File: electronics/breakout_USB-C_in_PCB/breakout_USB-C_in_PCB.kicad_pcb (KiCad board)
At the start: 2 copper layers, 29 x 29 mm, 20 parts, among them J1 USB-C_PD_USB, J2 Conn_02x05_Odd_Even

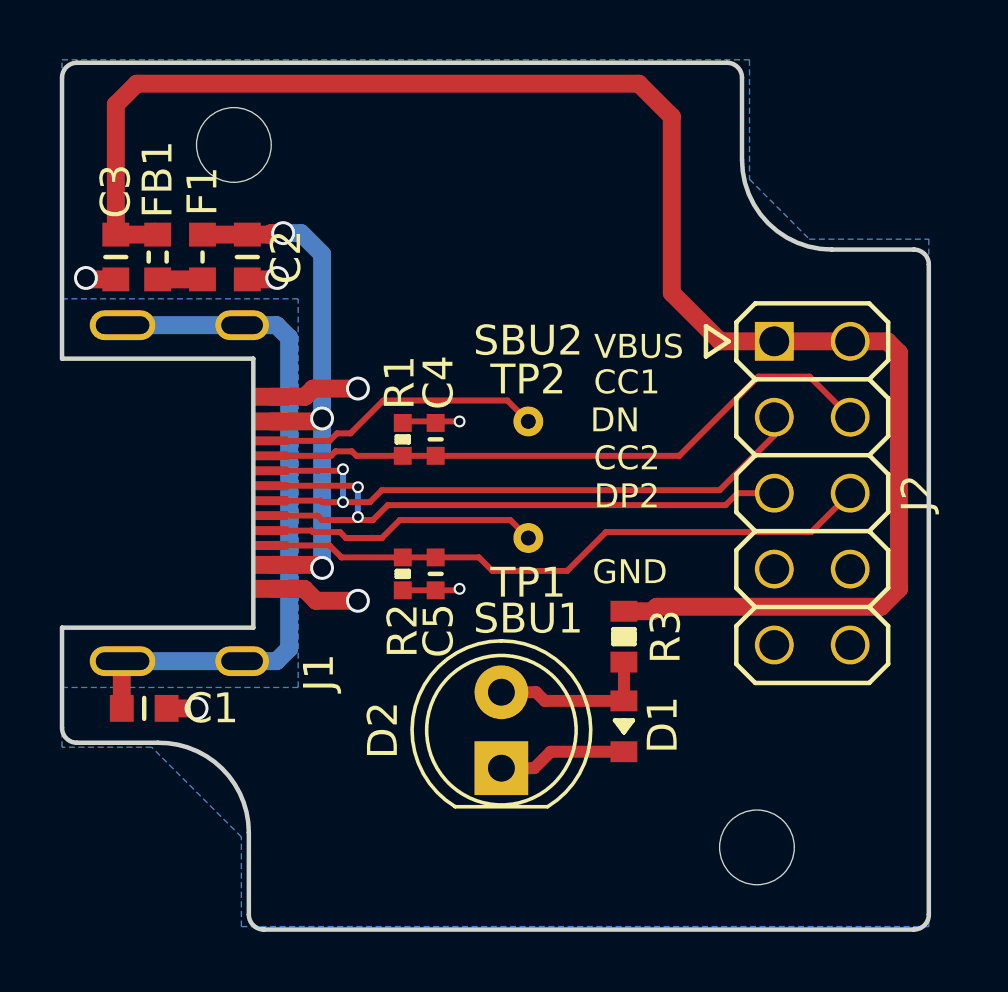
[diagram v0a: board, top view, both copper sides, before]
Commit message: updated versionnumber, usb data lines routing improved, led position and test pads updated
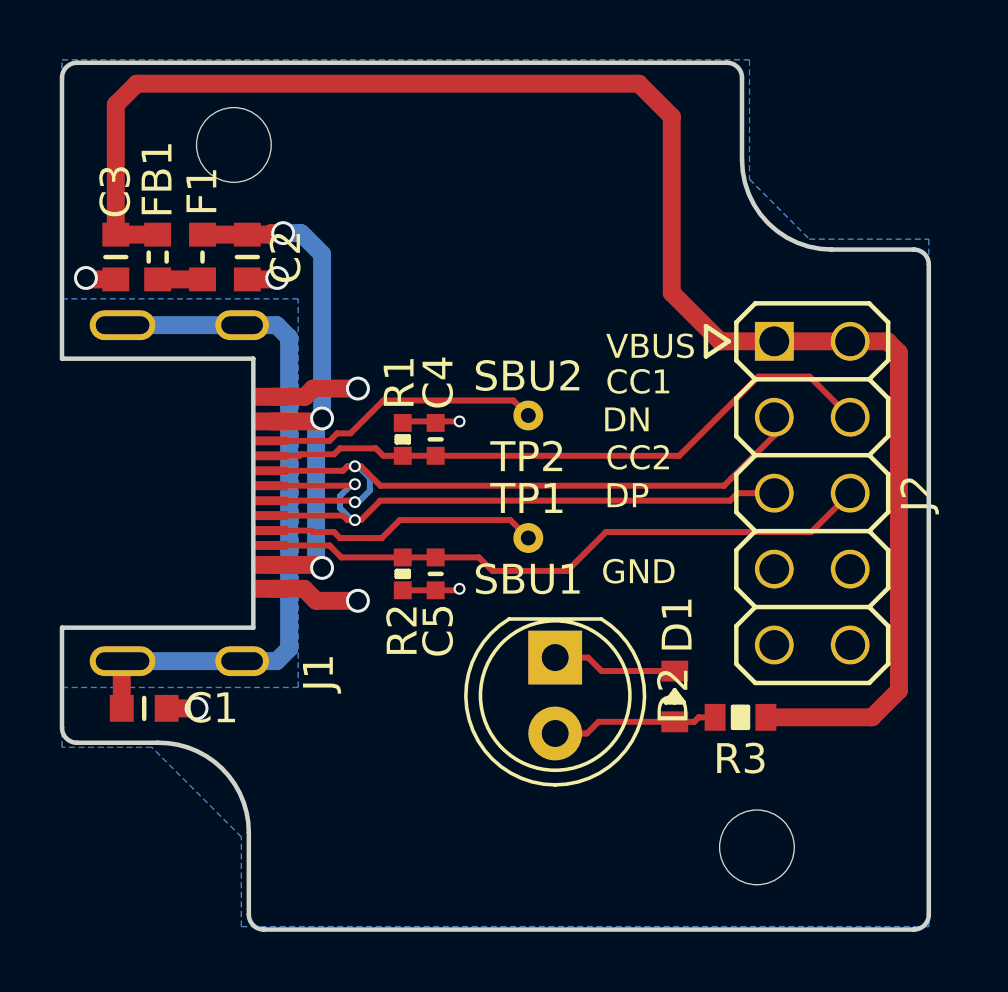
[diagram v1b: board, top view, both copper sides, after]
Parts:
- N2: value 20210610 -> 20210612
- moved R3 4.74 mm to (155.7, 109.0), turned to 180 degrees
- moved D2 4.11 mm to (149.5, 107.0), turned to 270 degrees
- moved D1 1.97 mm to (153.5, 108.3), turned to 270 degrees
- moved TP2 0.20 mm to (148.6, 98.9)
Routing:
- net /VCC: track 57.0 -> 55.7 mm
- net /DN: track 21.9 -> 23.0 mm
- net /DP: track 21.2 -> 21.8 mm
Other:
- board text added: "DP"
- board text removed: "DP2"

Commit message: silk mistake fixed, differential pair of usb optimized
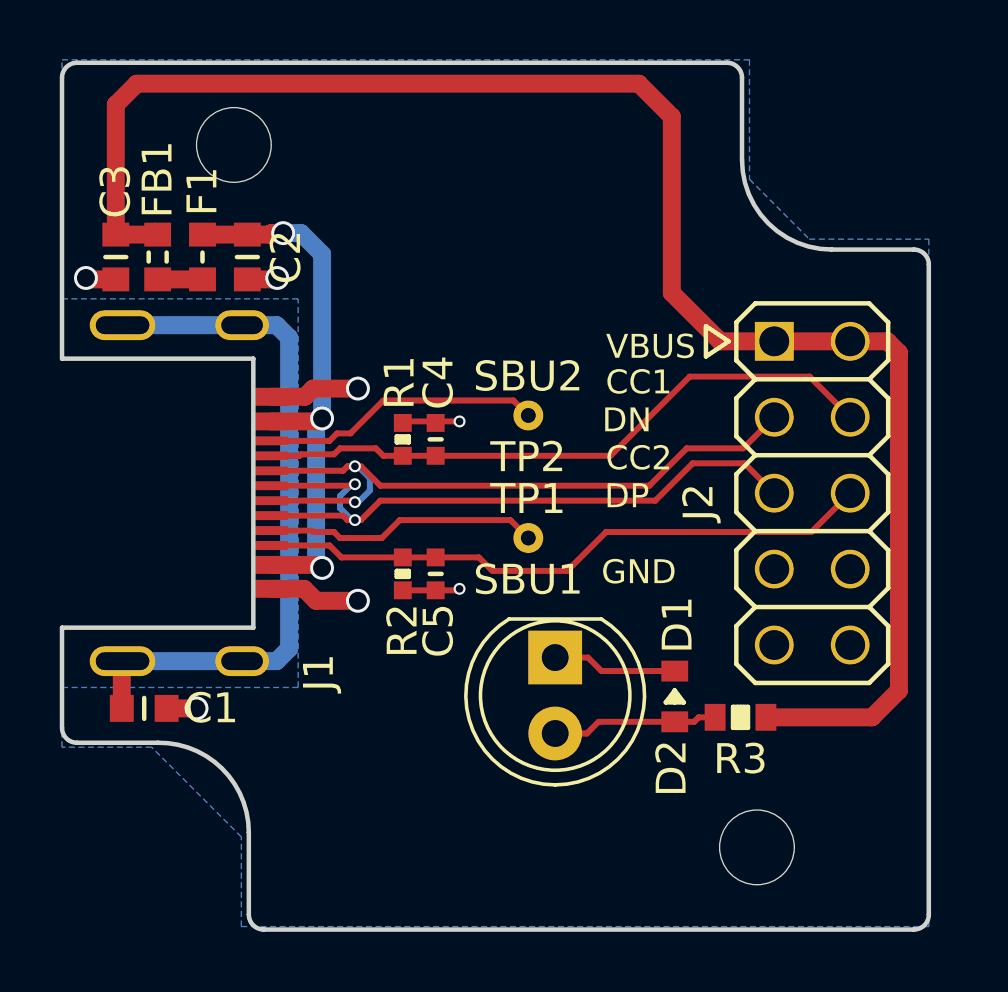
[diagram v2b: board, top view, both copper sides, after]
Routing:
- net /DP: track 21.8 -> 22.6 mm

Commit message: updated versionnumber, changed silk
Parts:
- N2: value 20210612 -> 20210613
